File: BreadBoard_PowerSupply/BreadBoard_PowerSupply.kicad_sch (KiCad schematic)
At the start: 17 parts, among them J1 Conn_01x02_Pin, J2 Conn_01x02_Pin, J3 Conn_01x03_Pin, J4 Conn_01x03_Pin, J5 Screw_Terminal_01x02, J6 Barrel_Jack_Switch, J7 Screw_Terminal_01x02, U1 LM7805_TO220, U2 LM317_TO-220

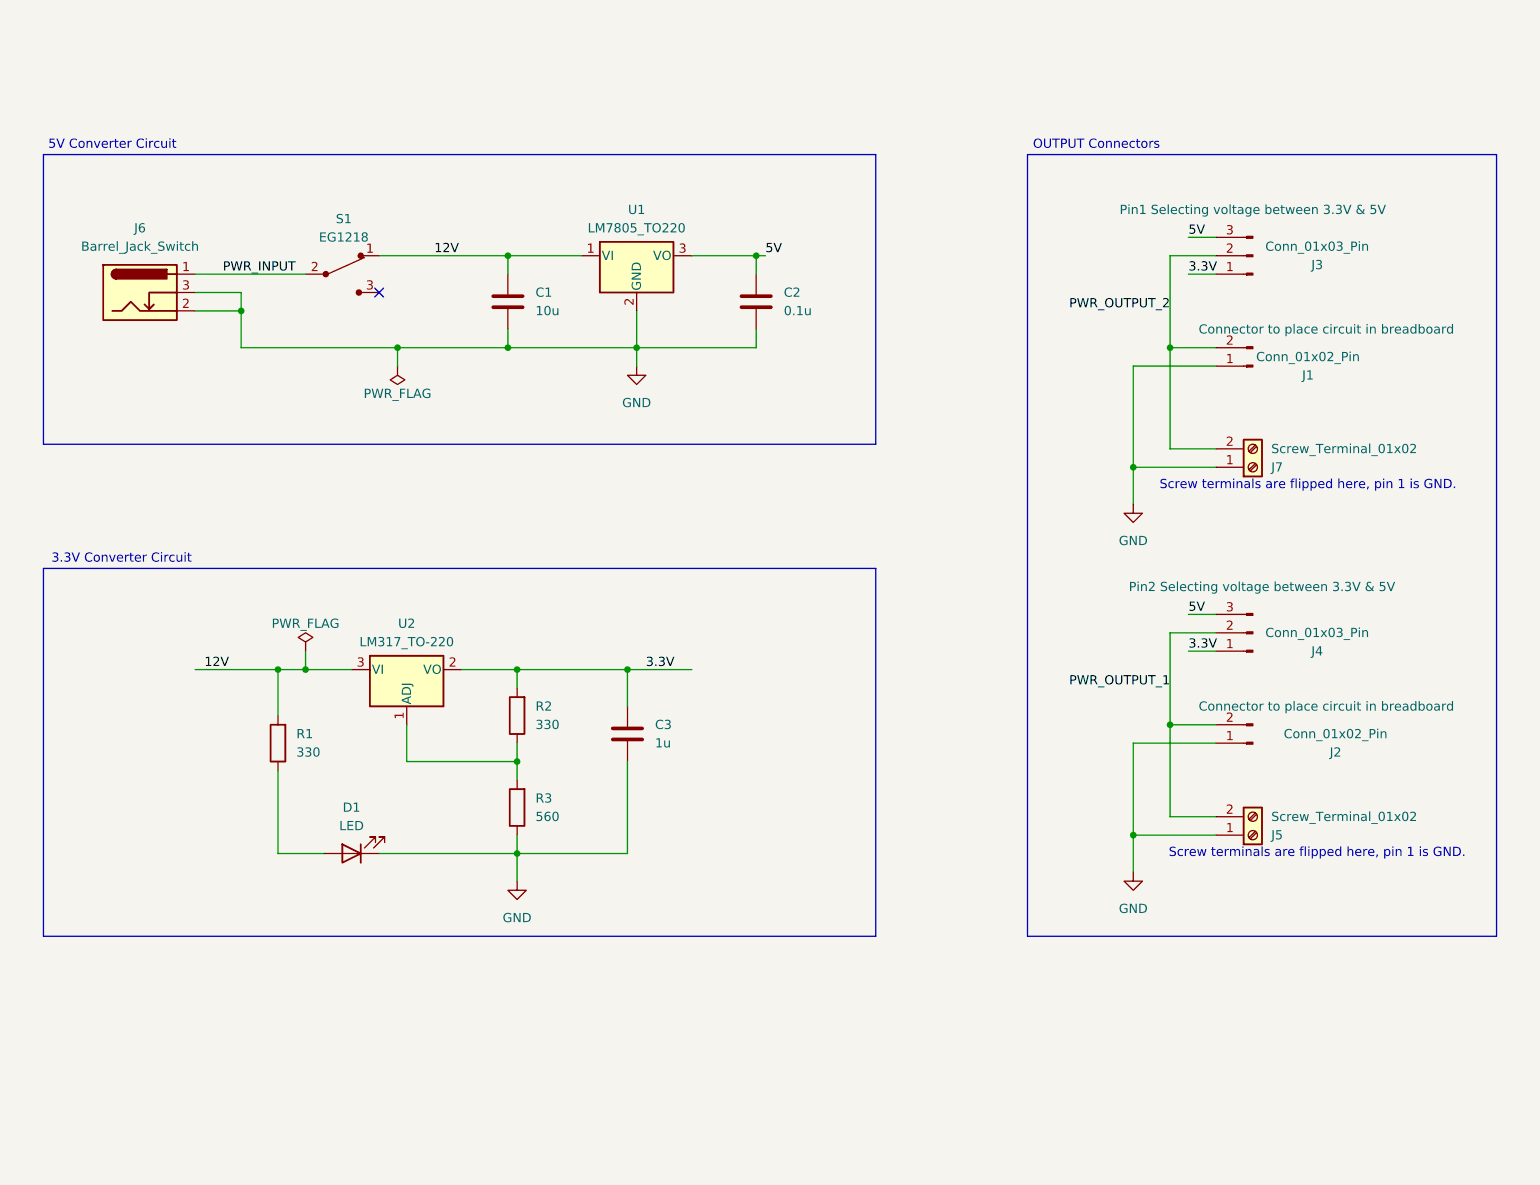
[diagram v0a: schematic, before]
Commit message: Updated
12V and 9V circuit added to schematics, components arranged on PCB,

Just have to confirm the sizes of components with available components in inventory and make the connections
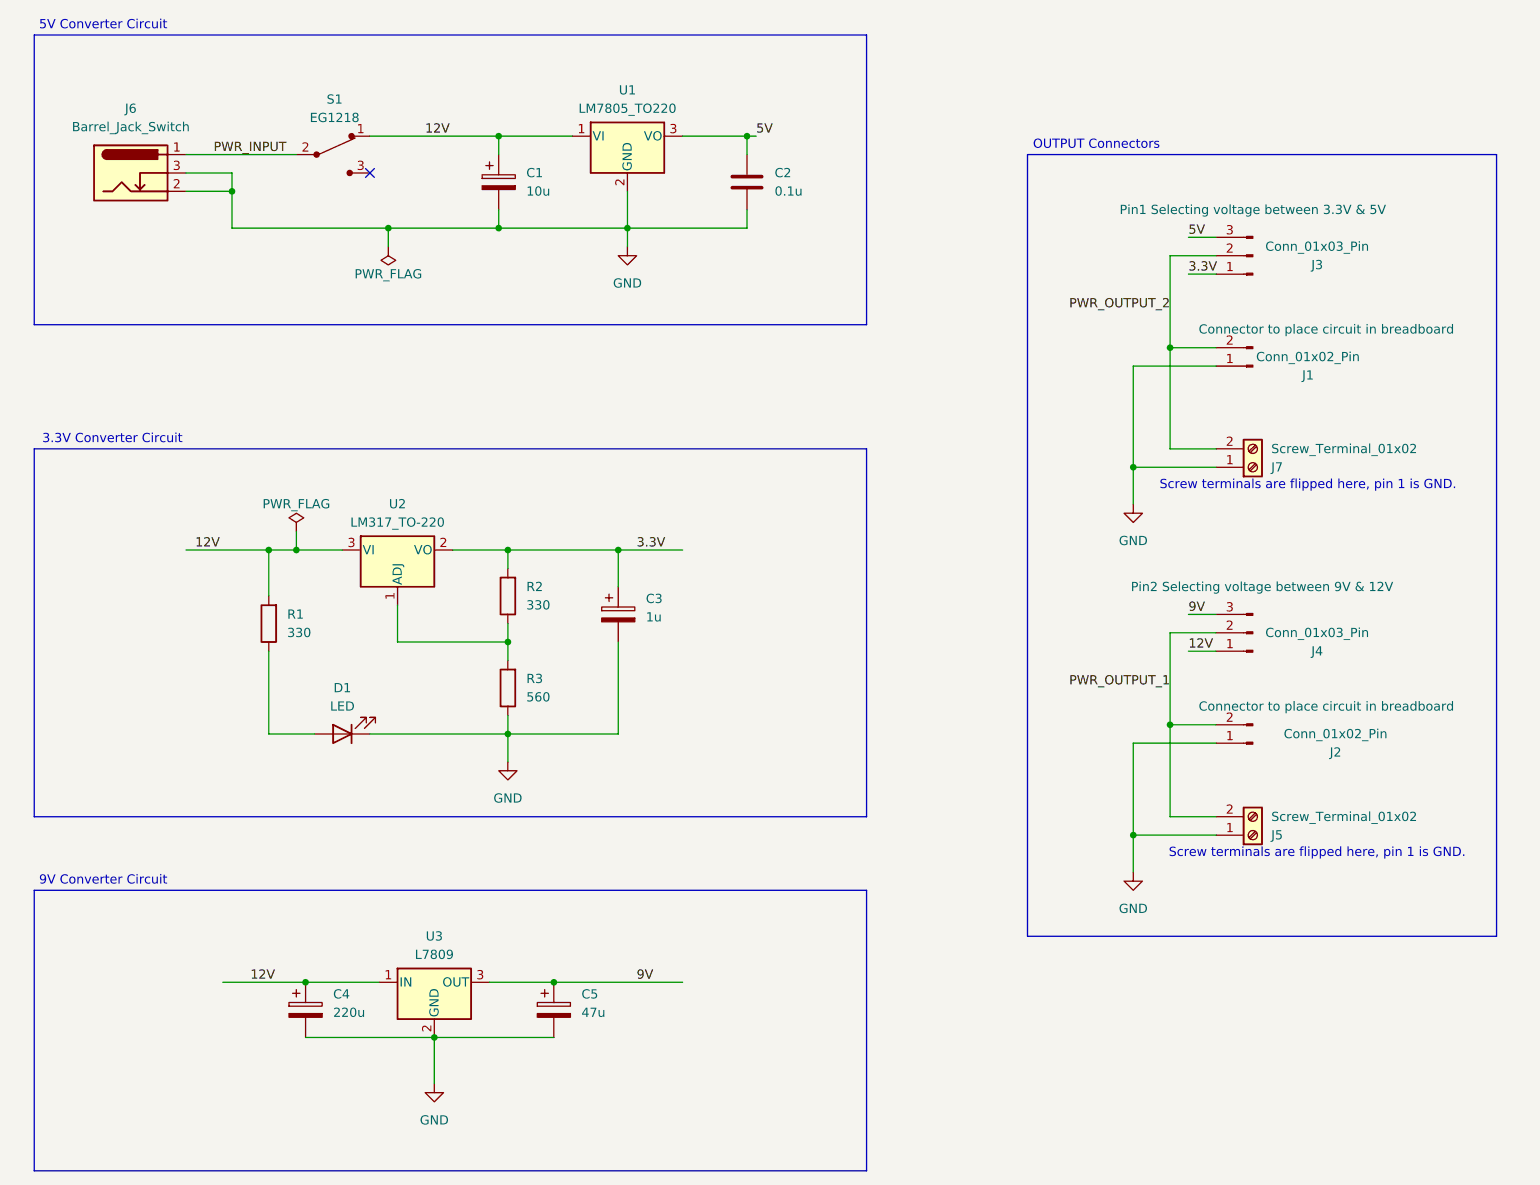
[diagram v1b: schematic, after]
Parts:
- added C4: 220u, Capacitor_THT:CP_Radial_D6.3mm_P2.50mm, symbol Device:C_Polarized
- added C5: 47u, Capacitor_THT:CP_Radial_D6.3mm_P2.50mm, symbol Device:C_Polarized
- added U3: L7809, L7809CV:TO255P1020X450X1968-3B, symbol Regulator_Linear:L7809
- C1, C3: footprint Capacitor_THT:C_Disc_D3.0mm_W1.6mm_P2.50mm -> Capacitor_THT:CP_Radial_D6.3mm_P2.50mm; symbol Device:C -> Device:C_Polarized
- J4: Purpose Pin2 Selecting voltage between 3.3V & 5V -> Pin2 Selecting voltage between 9V & 12V
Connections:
- net 12V: now also J4.1 (Pin_1), C4.1, U3.1 (IN)
- net 3.3V: now also C3.1; no longer C3.2, J4.1 (Pin_1)
- net 5V: no longer J4.3 (Pin_3)
- net GND: now also C3.2, C4.2, C5.2, U3.2 (GND); no longer C3.1
- new net 9V: C5.1, J4.3 (Pin_3), U3.3 (OUT)
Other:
- note added: "9V Converter Circuit"
- moved on the sheet: C2, D1, J6, R1, R2, R3, S1, U1, U2

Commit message: updates
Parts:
- added HS1, HS2, HS3: Heatsink, symbol Mechanical:Heatsink
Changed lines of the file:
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@@
+	)
+	(symbol
+		(lib_id "Mechanical:Heatsink")
+		(at 102.87 153.67 0)
+		(unit 1)
+		(exclude_from_sim yes)
+		(in_bom yes)
+		(on_board yes)
+		(dnp no)
+		(fields_autoplaced yes)
+		(property "Reference" "HS2"
+			(at 106.68 150.4949 0)
+			(effects
+				(font
+					(size 1.27 1.27)
+				)
+				(justify left)
+			)
+		)
+		(property "Value" "Heatsink"
+			(at 106.68 153.0349 0)
+			(effects
+				(font
+					(size 1.27 1.27)
+				)
+				(justify left)
+			)
+		)
+		(property "Footprint" ""
+			(at 103.1748 153.67 0)
+			(effects
+				(font
+					(size 1.27 1.27)
+				)
+				(hide yes)
+			)
+		)
+		(property "Datasheet" "~"
+			(at 103.1748 153.67 0)
+			(effects
+				(font
+					(size 1.27 1.27)
+				)
+				(hide yes)
+			)
+		)
+		(property "Description" "Heatsink"
+			(at 102.87 153.67 0)
+			(effects
+				(font
+					(size 1.27 1.27)
+				)
+				(hide yes)
+			)
+		)
+		(instances
+			(project "BreadBoard_PowerSupply"
+				(path "/2d0b1ab7-53aa-4650-a3ef-f0160e0df4b6"
+					(reference "HS2")
+					(unit 1)
+				)
+			)
+		)
 	)
 	(symbol
@@
 		(on_board yes)
 		(dnp no)
-		(fields_autoplaced yes)
 		(property "Reference" "U3"
-			(at 102.87 149.86 0)
+			(at 111.76 158.75 0)
 			(effects
 				(font
@@
 		)
 		(property "Value" "L7809"
-			(at 102.87 152.4 0)
+			(at 111.76 161.29 0)
 			(effects
 				(font
@@
 		(on_board yes)
 		(dnp no)
-		(fields_autoplaced yes)
 		(property "Reference" "U1"
-			(at 129.54 33.02 0)
+			(at 138.43 40.64 0)
 			(effects
 				(font
@@
 		)
 		(property "Value" "LM7805_TO220"
-			(at 129.54 35.56 0)
+			(at 138.43 43.18 0)
 			(effects
 				(font
@@
 		(dnp no)
 		(property "Reference" "U2"
-			(at 97.79 90.17 0)
+			(at 87.63 99.06 0)
 			(effects
 				(font
@@
 		)
 		(property "Value" "LM317_TO-220"
-			(at 97.79 92.71 0)
+			(at 87.63 101.6 0)
 			(effects
 				(font
@@
 	)
 	(symbol
+		(lib_id "Mechanical:Heatsink")
+		(at 97.79 93.98 0)
+		(unit 1)
+		(exclude_from_sim yes)
+		(in_bom yes)
+		(on_board yes)
+		(dnp no)
+		(fields_autoplaced yes)
+		(property "Reference" "HS1"
+			(at 101.6 90.8049 0)
+			(effects
+				(font
+					(size 1.27 1.27)
+				)
+				(justify left)
+			)
+		)
+		(property "Value" "Heatsink"
+			(at 101.6 93.3449 0)
+			(effects
+				(font
+					(size 1.27 1.27)
+				)
+				(justify left)
+			)
+		)
+		(property "Footprint" ""
+			(at 98.0948 93.98 0)
+			(effects
+				(font
+					(size 1.27 1.27)
+				)
+				(hide yes)
+			)
+		)
+		(property "Datasheet" "~"
+			(at 98.0948 93.98 0)
+			(effects
+				(font
+					(size 1.27 1.27)
+				)
+				(hide yes)
+			)
+		)
+		(property "Description" "Heatsink"
+			(at 97.79 93.98 0)
+			(effects
+				(font
+					(size 1.27 1.27)
+				)
+				(hide yes)
+			)
+		)
+		(instances
+			(project "BreadBoard_PowerSupply"
+				(path "/2d0b1ab7-53aa-4650-a3ef-f0160e0df4b6"
+					(reference "HS1")
+					(unit 1)
+				)
+			)
+		)
+	)
+	(symbol
 		(lib_id "power:PWR_FLAG")
 		(at 96.52 54.61 180)
@@
 					(unit 1)
 				)
+			)
+		)
+	)
+	(symbol
+		(lib_id "Mechanical:Heatsink")
+		(at 129.54 36.83 0)
+		(unit 1)
+		(exclude_from_sim yes)
+		(in_bom yes)
+		(on_board yes)
+		(dnp no)
+		(fields_autoplaced yes)
+		(property "Reference" "HS3"
+			(at 133.35 33.6549 0)
+			(effects
+				(font
+					(size 1.27 1.27)
+				)
+				(justify left)
+			)
+		)
+		(property "Value" "Heatsink"
+			(at 133.35 36.1949 0)
+			(effects
+				(font
+					(size 1.27 1.27)
+				)
+				(justify left)
+			)
+		)
+		(property "Footprint" ""
+			(at 129.8448 36.83 0)
+			(effects
+				(font
+					(size 1.27 1.27)
+				)
+				(hide yes)
+			)
+		)
+		(property "Datasheet" "~"
+			(at 129.8448 36.83 0)
+			(effects
+				(font
+					(size 1.27 1.27)
+				)
+				(hide yes)
+			)
+		)
+		(property "Description" "Heatsink"
+			(at 129.54 36.83 0)
+			(effects
+				(font
+					(size 1.27 1.27)
+				)
+				(hide yes)
+			)
+		)
+		(instances
+			(project ""
+				(path "/2d0b1ab7-53aa-4650-a3ef-f0160e0df4b6"
+					(reference "HS3")
+					(unit 1)
+				)
